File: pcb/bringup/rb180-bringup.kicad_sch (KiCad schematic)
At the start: 41 parts, among them J1 GT-USB-7010B, J2 Conn_02x03, J3 Conn_02x01, SW1 SKRPACE010, SW2 SKRPACE010, U2 NCP115ASN330, U4 W25Q128JVSS, Y1 12 MHz

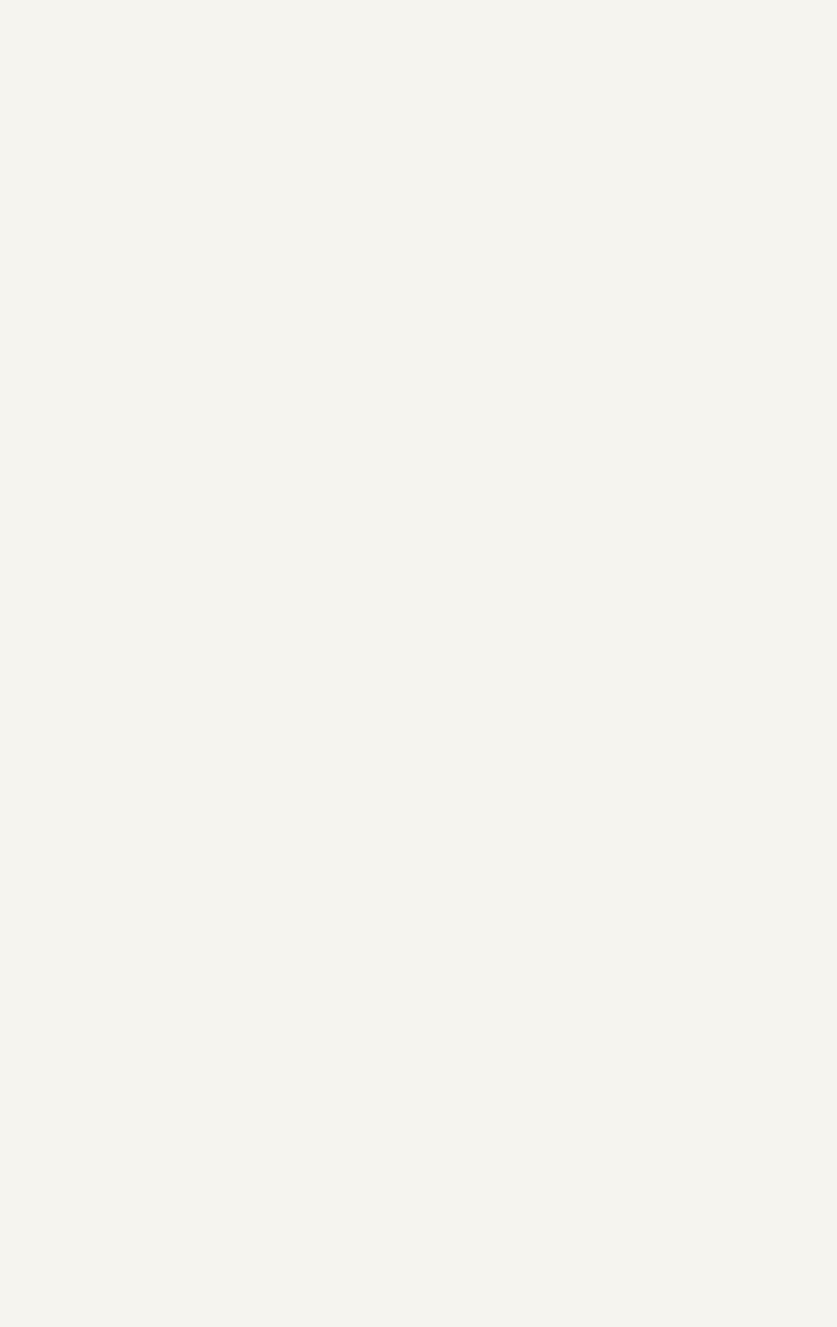
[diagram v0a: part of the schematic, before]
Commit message: Add async parallel SRAM symbol and wire it up to DUT
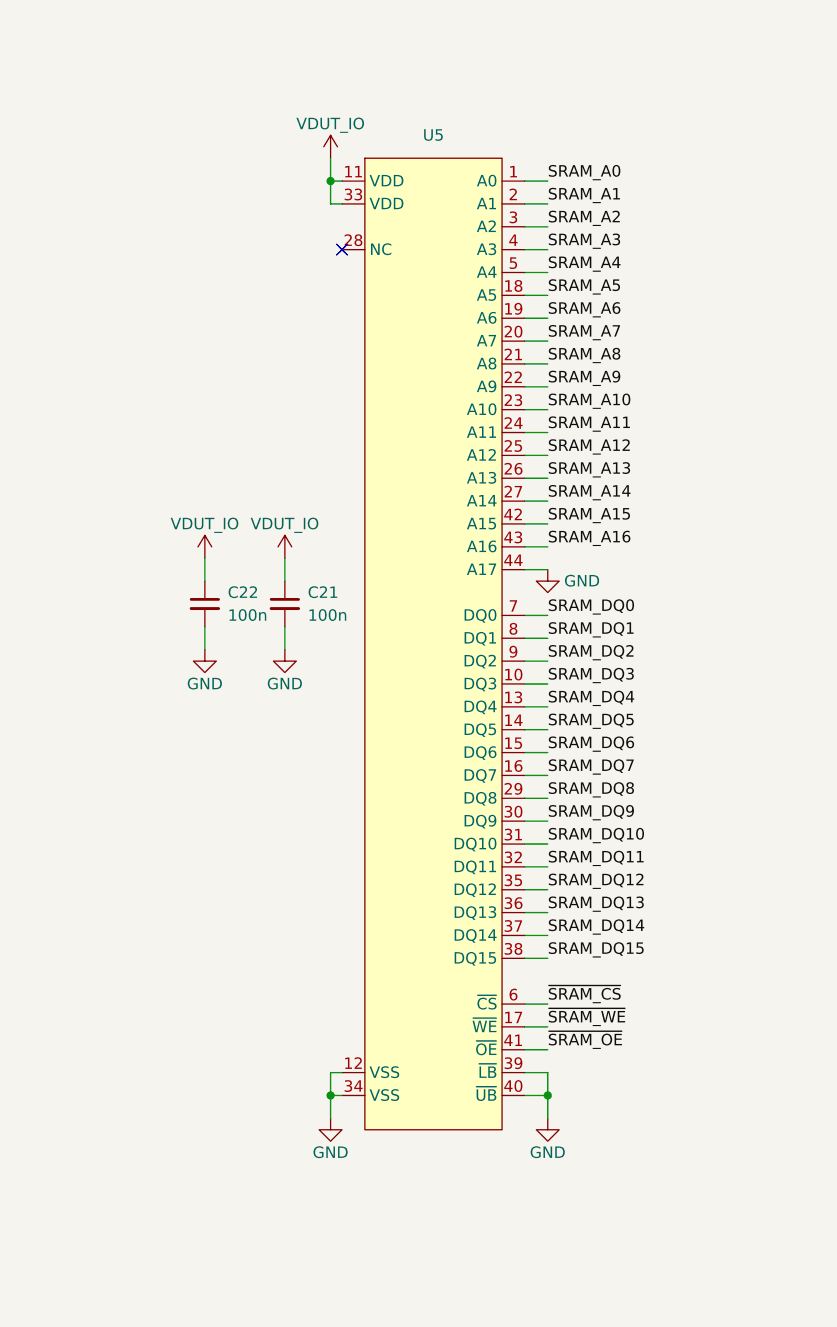
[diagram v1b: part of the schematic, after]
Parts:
- added C21, C22: 100n, Capacitor_SMD:C_0402_1005Metric, symbol Device:C_Small
- added U5: (no value), symbol rb180:R1RP0416DI
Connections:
- net GND: now also C21.2, C22.2, U5.12 (VSS), U5.34 (VSS), U5.39 (~{LB}), U5.40 (~{UB}), U5.44 (A17)
- net SRAM_A0: now also U5.1 (A0)
- net SRAM_A1: now also U5.2 (A1)
- net SRAM_A10: now also U5.23 (A10)
- net SRAM_A11: now also U5.24 (A11)
- net SRAM_A12: now also U5.25 (A12)
- net SRAM_A13: now also U5.26 (A13)
- net SRAM_A14: now also U5.27 (A14)
- net SRAM_A15: now also U5.42 (A15)
- net SRAM_A16: now also U5.43 (A16)
- net SRAM_A2: now also U5.3 (A2)
- net SRAM_A3: now also U5.4 (A3)
- net SRAM_A4: now also U5.5 (A4)
- net SRAM_A5: now also U5.18 (A5)
- net SRAM_A6: now also U5.19 (A6)
- net SRAM_A7: now also U5.20 (A7)
- net SRAM_A8: now also U5.21 (A8)
- net SRAM_A9: now also U5.22 (A9)
- net SRAM_DQ0: now also U5.7 (DQ0)
- net SRAM_DQ1: now also U5.8 (DQ1)
- net SRAM_DQ10: now also U5.31 (DQ10)
- net SRAM_DQ11: now also U5.32 (DQ11)
- net SRAM_DQ12: now also U5.35 (DQ12)
- net SRAM_DQ13: now also U5.36 (DQ13)
- net SRAM_DQ14: now also U5.37 (DQ14)
- net SRAM_DQ15: now also U5.38 (DQ15)
- net SRAM_DQ2: now also U5.9 (DQ2)
- net SRAM_DQ3: now also U5.10 (DQ3)
- net SRAM_DQ4: now also U5.13 (DQ4)
- net SRAM_DQ5: now also U5.14 (DQ5)
- net SRAM_DQ6: now also U5.15 (DQ6)
- net SRAM_DQ7: now also U5.16 (DQ7)
- net SRAM_DQ8: now also U5.29 (DQ8)
- net SRAM_DQ9: now also U5.30 (DQ9)
- net VDUT_IO: now also C21.1, C22.1, U5.11 (VDD), U5.33 (VDD)
- net ~{SRAM_CS}: now also U5.6 (~{CS})
- net ~{SRAM_OE}: now also U5.41 (~{OE})
- net ~{SRAM_WE}: now also U5.17 (~{WE})
- no-connect marks 2 -> 3

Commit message: Add level shifters
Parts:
- added C23, C24, C25, C26, C27, C28: 100n, Capacitor_SMD:C_0402_1005Metric, symbol Device:C_Small
- added R7: 470, Resistor_SMD:R_0402_1005Metric, symbol Device:R_Small
- added R8: 5k1, Resistor_SMD:R_0402_1005Metric, symbol Device:R_Small
- added U6, U7, U8: SN74LVC8T245, symbol Logic_LevelTranslator:SN74LVC8T245
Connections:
- net DUT_CLK: now also U8.7 (A5)
- net DUT_DCK: now also U8.10 (A8)
- net DUT_DIO: now also R7.2, U7.9 (A7)
- net GND: now also C23.2, C24.2, C25.2, C26.2, C27.2, C28.2, U6.11 (GND), U6.12 (GND), U6.13 (GND), U6.22 (~{OE}), U7.11 (GND), U7.12 (GND), U7.13 (GND), U7.22 (~{OE}), U8.11 (GND), U8.12 (GND), U8.13 (GND), U8.2 (DIR)
- net LCD_BL: now also U7.21 (B1); no longer U3.51 (LCD_BL)
- net LCD_CLK: now also U7.19 (B3); no longer U3.55 (LCD_CLK)
- net LCD_DAT0: now also U6.21 (B1); no longer U3.56 (LCD_DAT0)
- net LCD_DAT1: now also U6.20 (B2); no longer U3.57 (LCD_DAT1)
- net LCD_DAT2: now also U6.19 (B3); no longer U3.58 (LCD_DAT2)
- net LCD_DAT3: now also U6.18 (B4); no longer U3.59 (LCD_DAT3)
- net LCD_DAT4: now also U6.17 (B5); no longer U3.63 (LCD_DAT4)
- net LCD_DAT5: now also U6.16 (B6); no longer U3.64 (LCD_DAT5)
- net LCD_DAT6: now also U6.15 (B7); no longer U3.65 (LCD_DAT6)
- net LCD_DAT7: now also U6.14 (B8); no longer U3.66 (LCD_DAT7)
- net LCD_DC: now also U7.20 (B2); no longer U3.54 (LCD_DC)
- net PROBE_DCK: now also U8.14 (B8)
- net PROBE_DI: now also U7.15 (B7)
- net PROBE_DO: now also U8.15 (B7)
- net VDUT_IO: now also C23.1, C25.1, C27.1, U6.1 (V_{CCA}), U6.2 (DIR), U7.1 (V_{CCA}), U7.2 (DIR), U8.1 (V_{CCA})
- net PROBE_TO_DUT_SPARE2: now reaches U1.10 (GPIO7)
- net PROBE_TO_DUT_SPARE2: now also U8.19 (B3)
- net PROBE_TO_DUT_~{OE}: now reaches U1.12 (GPIO8)
- net PROBE_TO_DUT_~{OE}: now also R8.1, U8.22 (~{OE})
- net PROBE_TO_DUT_~{RST}: now reaches U1.16 (GPIO12)
- net PROBE_TO_DUT_~{RST}: now also U8.16 (B6)
- net PROBE_TO_DUT_CLK: now reaches U1.17 (GPIO13)
- net PROBE_TO_DUT_CLK: now also U8.17 (B5)
- net PROBE_TO_DUT_SPARE0: now reaches U1.8 (GPIO5)
- net PROBE_TO_DUT_SPARE0: now also U8.21 (B1)
- net PROBE_TO_DUT_SPARE1: now reaches U1.9 (GPIO6)
- net PROBE_TO_DUT_SPARE1: now also U8.20 (B2)
- net AUDIO renamed DUT_AUDIO
- net DUT_AUDIO: now also U7.10 (A8)
- net GPIO0 renamed DUT_MOSI
- net DUT_MOSI: now also U7.8 (A6)
- net GPIO1 renamed DUT_SCK
- net DUT_SCK: now also U7.7 (A5)
- net GPIO2 renamed DUT_~{CS}
- net DUT_~{CS}: now also U7.6 (A4)
- net GPIO3 renamed DUT_MISO
- net DUT_MISO: now also U8.6 (A4)
- new net: R7.1, U8.9 (A7)
- new net 3V3: C24.1, C26.1, C28.1, R8.2, U6.23 (V_{CCB}), U6.24 (V_{CCB}), U7.23 (V_{CCB}), U7.24 (V_{CCB}), U8.23 (V_{CCB}), U8.24 (V_{CCB})
- new net AUDIO_PWM: U7.14 (B8)
- new net DUT_LCD_BL: U3.51 (LCD_BL), U7.3 (A1)
- new net DUT_LCD_CLK: U3.55 (LCD_CLK), U7.5 (A3)
- new net DUT_LCD_DAT0: U3.56 (LCD_DAT0), U6.3 (A1)
- new net DUT_LCD_DAT1: U3.57 (LCD_DAT1), U6.4 (A2)
- new net DUT_LCD_DAT2: U3.58 (LCD_DAT2), U6.5 (A3)
- new net DUT_LCD_DAT3: U3.59 (LCD_DAT3), U6.6 (A4)
- new net DUT_LCD_DAT4: U3.63 (LCD_DAT4), U6.7 (A5)
- new net DUT_LCD_DAT5: U3.64 (LCD_DAT5), U6.8 (A6)
- new net DUT_LCD_DAT6: U3.65 (LCD_DAT6), U6.9 (A7)
- new net DUT_LCD_DAT7: U3.66 (LCD_DAT7), U6.10 (A8)
- new net DUT_LCD_DC: U3.54 (LCD_DC), U7.4 (A2)
- new net DUT_SPARE0: U8.3 (A1)
- new net DUT_SPARE1: U8.4 (A2)
- new net DUT_SPARE2: U8.5 (A3)
- new net DUT_~{RST}: U8.8 (A6)
- new net FLASH_MISO: U8.18 (B4)
- new net FLASH_MOSI: U7.16 (B6)
- new net FLASH_SCK: U7.17 (B5)
- new net FLASH_~{CS}: U7.18 (B4)
- no-connect marks 3 -> 4
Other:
- note added: "DIR = 0: A <- B DIR = 1: A -> B"
- note added: "Debug Probe (RP2350)"
- note added: "GP13 is clock GPOUT0"
- note added: "Level Shifters"
- note added: "SRAM"
- note added: "Signals *from* DUT"
- note added: "Signals *to* DUT"
- note added: "Unused tied to GND on both sides (per datasheet)"
- note removed: "Debug Probe"
- moved on the sheet: C1, C10, C11, C12, C13, C14, C15, C16, C17, C18, C19, C2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
